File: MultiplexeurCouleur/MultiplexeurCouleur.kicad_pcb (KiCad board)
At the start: 4 copper layers, 49.5 x 33.8 mm, 29 parts, among them J1 Color0, J2 Color1, J3 Color2, J4 Color3, J5 Color4, J6 Color5, J7 Color6, J8 Color7, J9 Interf ARIG, U1 TCA9548APWR

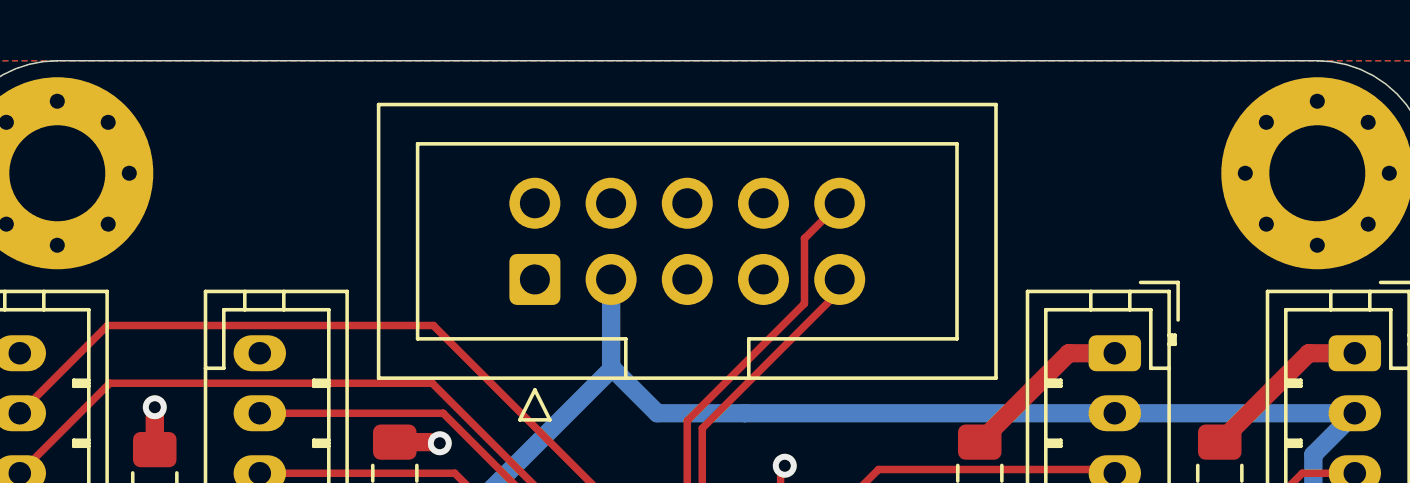
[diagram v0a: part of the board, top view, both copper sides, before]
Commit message: Ajout bornier alim 5V sur multiplexeur couleur
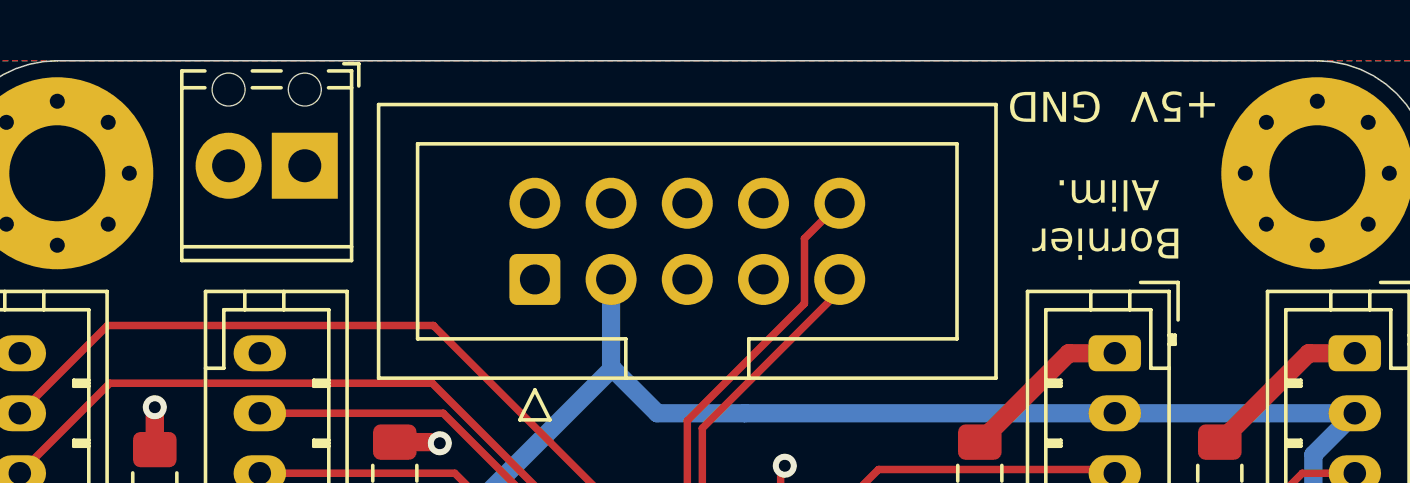
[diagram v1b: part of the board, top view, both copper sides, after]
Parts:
- added J10: Alim 5V, TerminalBlock_Phoenix:TerminalBlock_Phoenix_MPT-0,5-2-2.54_1x02_P2.54mm_Horizontal, F.Cu at (128.5, 68.2)
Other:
- board text added: "+5V"
- board text added: "Bornier Alim."
- board text added: "GND"
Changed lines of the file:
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@@
-(kicad_pcb (version 20171130) (host pcbnew 5.1.9-1.fc32)
+(kicad_pcb (version 20171130) (host pcbnew 5.1.9-1.fc33)
   (general
     (thickness 1.6)
-    (drawings 9)
+    (drawings 12)
     (tracks 167)
     (zones 0)
-    (modules 29)
+    (modules 30)
     (nets 31)
   )
@@
     (add_net SDA6)
     (add_net SDA7)
+  )
+  (module TerminalBlock_Phoenix:TerminalBlock_Phoenix_MPT-0,5-2-2.54_1x02_P2.54mm_Horizontal (layer F.Cu)
+    (at 128.5 68.25 180)
+    (descr "Terminal Block Phoenix MPT-0,5-2-2.54, 2 pins, pitch 2.54mm, size 5.54x6.2mm^2, drill diamater 1.1mm, pad diameter 2.2mm, see http://www.mouser.com/ds/2/324/ItemDetail_1725656-920552.pdf, script-generated using https://github.com/pointhi/kicad-footprint-generator/scripts/TerminalBlock_Phoenix")
+    (tags "THT Terminal Block Phoenix MPT-0,5-2-2.54 pitch 2.54mm size 5.54x6.2mm^2 drill 1.1mm pad 2.2mm")
+    (fp_text reference J10 (at 1.27 -4.16) (layer F.SilkS) hide
+      (effects (font (size 1 1) (thickness 0.15)))
+    )
+    (fp_text value "Alim 5V" (at 1.27 4.16) (layer F.Fab)
+      (effects (font (size 1 1) (thickness 0.15)))
+    )
+    (fp_line (start 4.54 -3.6) (end -2 -3.6) (layer F.CrtYd) (width 0.05))
+    (fp_line (start 4.54 3.6) (end 4.54 -3.6) (layer F.CrtYd) (width 0.05))
+    (fp_line (start -2 3.6) (end 4.54 3.6) (layer F.CrtYd) (width 0.05))
+    (fp_line (start -2 -3.6) (end -2 3.6) (layer F.CrtYd) (width 0.05))
+    (fp_line (start -1.8 3.4) (end -1.3 3.4) (layer F.SilkS) (width 0.12))
+    (fp_line (start -1.8 2.66) (end -1.8 3.4) (layer F.SilkS) (width 0.12))
+    (fp_line (start 3.241 -0.835) (end 1.706 0.7) (layer F.Fab) (width 0.1))
+    (fp_line (start 3.375 -0.7) (end 1.84 0.835) (layer F.Fab) (width 0.1))
+    (fp_line (start 0.701 -0.835) (end -0.835 0.7) (layer F.Fab) (width 0.1))
+    (fp_line (start 0.835 -0.7) (end -0.701 0.835) (layer F.Fab) (width 0.1))
+    (fp_line (start 4.1 -3.16) (end 4.1 3.16) (layer F.SilkS) (width 0.12))
+    (fp_line (start -1.56 -3.16) (end -1.56 3.16) (layer F.SilkS) (width 0.12))
+    (fp_line (start 3.33 3.16) (end 4.1 3.16) (layer F.SilkS) (width 0.12))
+    (fp_line (start 0.79 3.16) (end 1.75 3.16) (layer F.SilkS) (width 0.12))
+    (fp_line (start -1.56 3.16) (end -0.79 3.16) (layer F.SilkS) (width 0.12))
+    (fp_line (start -1.56 -3.16) (end 4.1 -3.16) (layer F.SilkS) (width 0.12))
+    (fp_line (start -1.56 -2.7) (end 4.1 -2.7) (layer F.SilkS) (width 0.12))
+    (fp_line (start -1.5 -2.7) (end 4.04 -2.7) (layer F.Fab) (width 0.1))
+    (fp_line (start 3.33 2.6) (end 4.1 2.6) (layer F.SilkS) (width 0.12))
+    (fp_line (start 0.79 2.6) (end 1.75 2.6) (layer F.SilkS) (width 0.12))
+    (fp_line (start -1.56 2.6) (end -0.79 2.6) (layer F.SilkS) (width 0.12))
+    (fp_line (start -1.5 2.6) (end 4.04 2.6) (layer F.Fab) (width 0.1))
+    (fp_line (start -1.5 2.6) (end -1.5 -3.1) (layer F.Fab) (width 0.1))
+    (fp_line (start -1 3.1) (end -1.5 2.6) (layer F.Fab) (width 0.1))
+    (fp_line (start 4.04 3.1) (end -1 3.1) (layer F.Fab) (width 0.1))
+    (fp_line (start 4.04 -3.1) (end 4.04 3.1) (layer F.Fab) (width 0.1))
+    (fp_line (start -1.5 -3.1) (end 4.04 -3.1) (layer F.Fab) (width 0.1))
+    (fp_circle (center 2.54 0) (end 3.64 0) (layer F.Fab) (width 0.1))
+    (fp_circle (center 0 0) (end 1.1 0) (layer F.Fab) (width 0.1))
+    (fp_text user %R (at 1.27 2) (layer F.Fab)
+      (effects (font (size 1 1) (thickness 0.15)))
+    )
+    (pad "" np_thru_hole circle (at 2.54 2.54 180) (size 1.1 1.1) (drill 1.1) (layers *.Cu *.Mask))
+    (pad 2 thru_hole circle (at 2.54 0 180) (size 2.2 2.2) (drill 1.1) (layers *.Cu *.Mask)
+      (net 1 GND))
+    (pad "" np_thru_hole circle (at 0 2.54 180) (size 1.1 1.1) (drill 1.1) (layers *.Cu *.Mask))
+    (pad 1 thru_hole rect (at 0 0 180) (size 2.2 2.2) (drill 1.1) (layers *.Cu *.Mask)
+      (net 2 +5V))
+    (model ${KISYS3DMOD}/TerminalBlock_Phoenix.3dshapes/TerminalBlock_Phoenix_MPT-0,5-2-2.54_1x02_P2.54mm_Horizontal.wrl
+      (at (xyz 0 0 0))
+      (scale (xyz 1 1 1))
+      (rotate (xyz 0 0 0))
+    )
   )
   (module ARIG:Logo_ARIG_12_6x6_6 locked (layer B.Cu)
@@
     )
   )
+  (gr_text "Bornier\nAlim." (at 155.25 70 180) (layer F.SilkS)
+    (effects (font (size 1 1) (thickness 0.15)))
+  )
+  (gr_text +5V (at 157.5 66.25 180) (layer F.SilkS)
+    (effects (font (size 1 1) (thickness 0.15)))
+  )
+  (gr_text GND (at 153.5 66.25 180) (layer F.SilkS)
+    (effects (font (size 1 1) (thickness 0.15)))
+  )
   (gr_text "Multiplexeur I2C\n2021" (at 141.25 87.75) (layer B.SilkS)

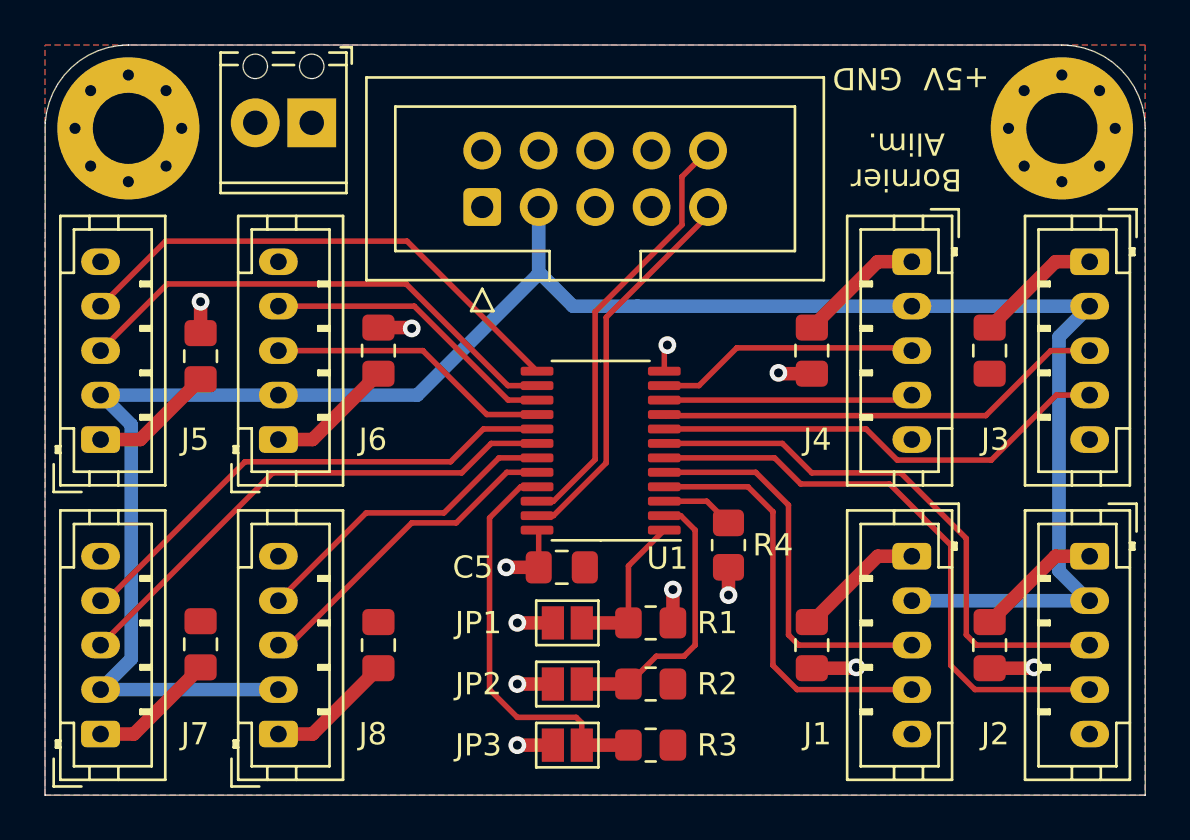
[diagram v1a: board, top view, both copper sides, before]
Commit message: Finalisation multiplexeur couleur
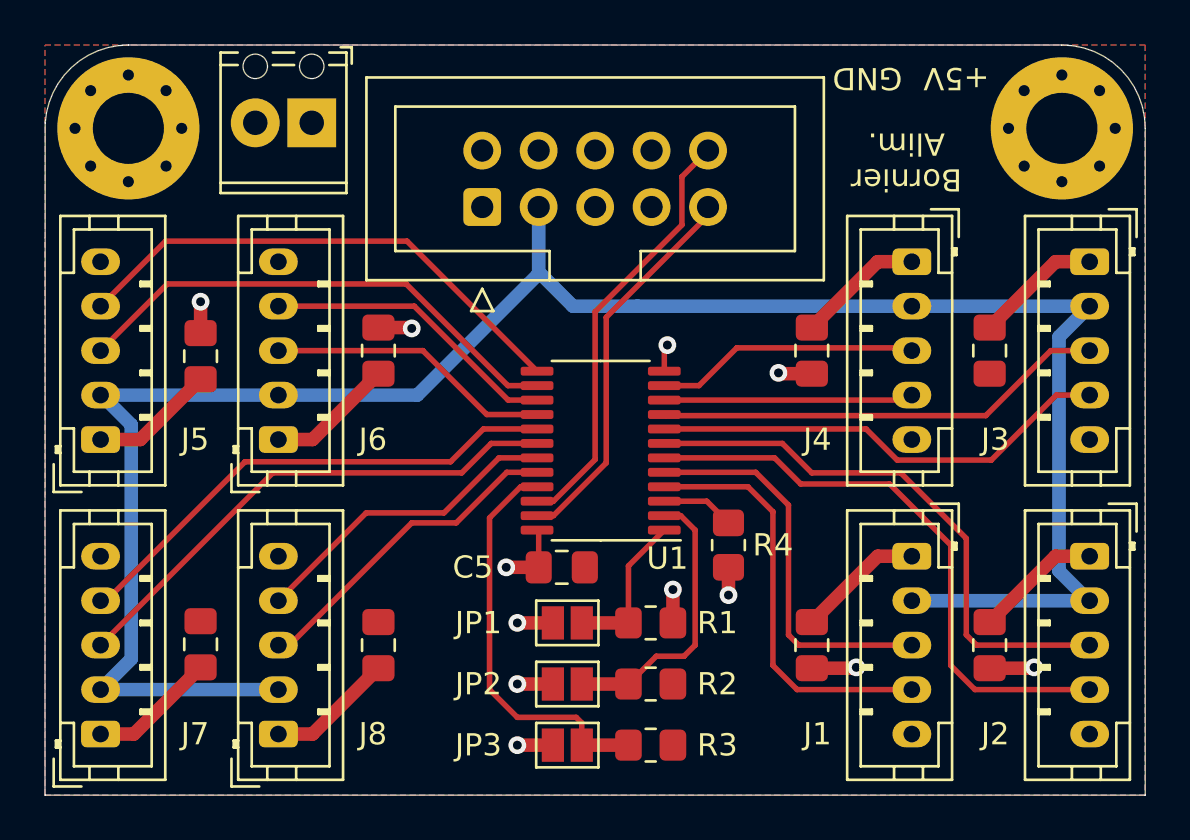
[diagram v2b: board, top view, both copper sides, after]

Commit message: Convert old schematics
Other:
- net class Default removed
